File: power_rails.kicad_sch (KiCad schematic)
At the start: 31 parts, among them SW3 ~{SR}, SW4 ~{PB}, U12 MCP1799T-5002H/TT, U5 AP63200WU, U7 AP63205WU, U8 STM6601CM2DDM6F, U9 TPS62162DSG

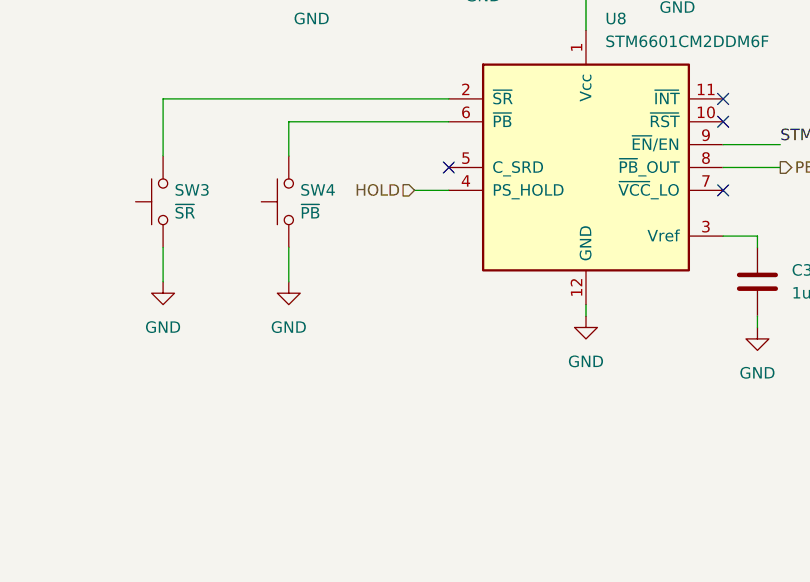
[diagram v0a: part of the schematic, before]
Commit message: feat: switch to 4-layers and layout improvements
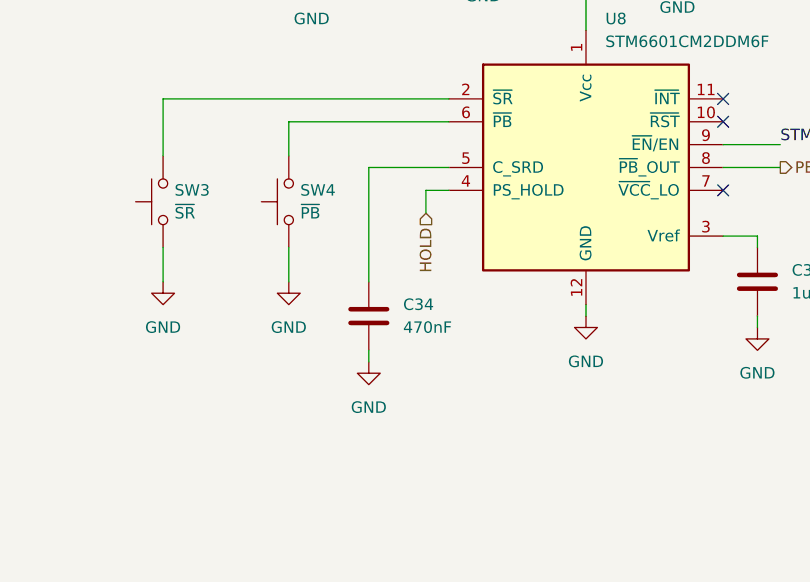
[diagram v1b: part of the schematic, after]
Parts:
- added C34: 470nF, Capacitor_SMD:C_0603_1608Metric, symbol Device:C
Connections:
- net GND: now also C34.2
- net at U8.5 (C_SRD): now also C34.1
- no-connect marks 4 -> 3
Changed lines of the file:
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@@
 		(at 260.35 106.68)
 	)
-	(no_connect
-		(at 229.87 104.14)
-	)
 	(wire
 		(pts
@@
 	(wire
 		(pts
+			(xy 227.33 109.22) (xy 227.33 106.68)
+		)
+		(stroke
+			(width 0)
+			(type default)
+		)
+	)
+	(wire
+		(pts
 			(xy 121.92 29.21) (xy 121.92 35.56)
 		)
@@
 	(wire
 		(pts
+			(xy 220.98 104.14) (xy 229.87 104.14)
+		)
+		(stroke
+			(width 0)
+			(type default)
+		)
+	)
+	(wire
+		(pts
 			(xy 107.95 153.67) (xy 110.49 153.67)
 		)
@@
 	(wire
 		(pts
-			(xy 226.06 106.68) (xy 229.87 106.68)
+			(xy 220.98 116.84) (xy 220.98 104.14)
 		)
 		(stroke
@@
 	(wire
 		(pts
+			(xy 220.98 124.46) (xy 220.98 125.73)
+		)
+		(stroke
+			(width 0)
+			(type default)
+		)
+	)
+	(wire
+		(pts
 			(xy 110.49 153.67) (xy 116.84 153.67)
 		)
@@
 	(wire
 		(pts
+			(xy 227.33 106.68) (xy 229.87 106.68)
+		)
+		(stroke
+			(width 0)
+			(type default)
+		)
+	)
+	(wire
+		(pts
 			(xy 214.63 71.12) (xy 214.63 68.58)
 		)
@@
 	(hierarchical_label "HOLD"
 		(shape input)
-		(at 226.06 106.68 180)
+		(at 227.33 109.22 270)
 		(effects
 			(font
@@
 	)
 	(symbol
+		(lib_id "Device:C")
+		(at 220.98 120.65 0)
+		(unit 1)
+		(body_style 1)
+		(exclude_from_sim no)
+		(in_bom yes)
+		(on_board yes)
+		(in_pos_files yes)
+		(dnp no)
+		(fields_autoplaced yes)
+		(property "Reference" "C34"
+			(at 224.79 119.3799 0)
+			(show_name no)
+			(do_not_autoplace no)
+			(effects
+				(font
+					(size 1.27 1.27)
+				)
+				(justify left)
+			)
+		)
+		(property "Value" "470nF"
+			(at 224.79 121.9199 0)
+			(show_name no)
+			(do_not_autoplace no)
+			(effects
+				(font
+					(size 1.27 1.27)
+				)
+				(justify left)
+			)
+		)
+		(property "Footprint" "Capacitor_SMD:C_0603_1608Metric"
+			(at 221.9452 124.46 0)
+			(hide yes)
+			(show_name no)
+			(do_not_autoplace no)
+			(effects
+				(font
+					(size 1.27 1.27)
+				)
+			)
+		)
+		(property "Datasheet" "https://datasheet.lcsc.com/datasheet/pdf/02336ea48ea44ca18c72517dd3cb7b47.pdf?productCode=C5673"
+			(at 220.98 120.65 0)
+			(hide yes)
+			(show_name no)
+			(do_not_autoplace no)
+			(effects
+				(font
+					(size 1.27 1.27)
+				)
+			)
+		)
+		(property "Description" "Unpolarized capacitor"
+			(at 220.98 120.65 0)
+			(hide yes)
+			(show_name no)
+			(do_not_autoplace no)
+			(effects
+				(font
+					(size 1.27 1.27)
+				)
+			)
+		)
+		(property "LCSC" "C1623"
+			(at -43.18 3.81 0)
+			(hide yes)
+			(show_name no)
+			(do_not_autoplace no)
+			(effects
+				(font
+					(size 1.27 1.27)
+				)
+			)
+		)
+		(property "MPN" ""
+			(at -43.18 3.81 0)
+			(hide yes)
+			(show_name no)
+			(do_not_autoplace no)
+			(effects
+				(font
+					(size 1.27 1.27)
+				)
+			)
+		)
+		(property "Manufacturer" "Generic"
+			(at -43.18 3.81 0)
+			(hide yes)
+			(show_name no)
+			(do_not_autoplace no)
+			(effects
+				(font
+					(size 1.27 1.27)
+				)
+			)
+		)
+		(pin "1"
+		)
+		(pin "2"
+		)
+		(instances
+			(project "rover-circuit"
+				(path "/0461baee-3b25-4e1a-a5c1-d76b4b99c66c/f4b194fd-8f48-4986-9deb-ce512b0299fe"
+					(reference "C34")
+					(unit 1)
+				)
+			)
+		)
+	)
+	(symbol
 		(lib_id "power:GND")
 		(at 123.19 111.76 0)
@@
 					(unit 1)
 				)
+			)
+		)
+	)
+	(symbol
+		(lib_id "power:GND")
+		(at 220.98 125.73 0)
+		(unit 1)
+		(body_style 1)
+		(exclude_from_sim no)
+		(in_bom yes)
+		(on_board yes)
+		(in_pos_files yes)
+		(dnp no)
+		(fields_autoplaced yes)
+		(property "Reference" "#PWR096"
+			(at 220.98 132.08 0)
+			(hide yes)
+			(show_name no)
+			(do_not_autoplace no)
+			(effects
+				(font
+					(size 1.27 1.27)
+				)
+			)
+		)
+		(property "Value" "GND"
+			(at 220.98 130.81 0)
+			(show_name no)
+			(do_not_autoplace no)
+			(effects
+				(font
+					(size 1.27 1.27)
+				)
+			)
+		)
+		(property "Footprint" ""
+			(at 220.98 125.73 0)
+			(hide yes)
+			(show_name no)
+			(do_not_autoplace no)
+			(effects
+				(font
+					(size 1.27 1.27)
+				)
+			)
+		)
+		(property "Datasheet" ""
+			(at 220.98 125.73 0)
+			(hide yes)
+			(show_name no)
+			(do_not_autoplace no)
+			(effects
+				(font
+					(size 1.27 1.27)
+				)
+			)
+		)
+		(property "Description" "Power symbol creates a global label with name \"GND\" , ground"
+			(at 220.98 125.73 0)
+			(hide yes)
+			(show_name no)
+			(do_not_autoplace no)
+			(effects
+				(font
+					(size 1.27 1.27)
+				)
+			)
+		)
+		(pin "1"
+		)
+		(instances
+			(project "rover-circuit"
+				(path "/0461baee-3b25-4e1a-a5c1-d76b4b99c66c/f4b194fd-8f48-4986-9deb-ce512b0299fe"
+					(reference "#PWR096")
+					(unit 1)
+				)
